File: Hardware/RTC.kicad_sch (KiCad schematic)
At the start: 13 parts

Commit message: add diode
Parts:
- added D? (x3): D_Schottky, symbol IVS_SYMBOL_DIR:D_Schottky
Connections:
- net +3V3: now also D?.1, D?.1
- net at IC?.14 (VBAT): now also D?.2, D?.2
- net at BT?.1 (+), R?.1, R?.2: now also D?.2
- net at BT?.1 (+): now also D?.1
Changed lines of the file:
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@@
   (junction (at 80.01 67.31) (diameter 0) (color 0 0 0 0)
+  )
+  (junction (at 113.03 88.9) (diameter 0) (color 0 0 0 0)
   )
   (junction (at 97.79 88.9) (diameter 0) (color 0 0 0 0)
@@
     (stroke (width 0) (type default) (color 0 0 0 0))
   )
-  (wire (pts (xy 100.33 88.9) (xy 109.22 88.9))
+  (wire (pts (xy 100.33 88.9) (xy 113.03 88.9))
     (stroke (width 0) (type default) (color 0 0 0 0))
   )
@@
     (stroke (width 0) (type default) (color 0 0 0 0))
   )
+  (wire (pts (xy 113.03 96.52) (xy 119.38 96.52))
+    (stroke (width 0) (type default) (color 0 0 0 0))
+  )
   (wire (pts (xy 76.2 106.68) (xy 87.63 106.68))
     (stroke (width 0) (type default) (color 0 0 0 0))
@@
     (stroke (width 0) (type default) (color 0 0 0 0))
   )
-  (wire (pts (xy 116.84 88.9) (xy 125.73 88.9))
-    (stroke (width 0) (type default) (color 0 0 0 0))
-  )
   (wire (pts (xy 85.09 57.785) (xy 86.36 57.785))
     (stroke (width 0) (type default) (color 0 0 0 0))
@@
     (stroke (width 0) (type default) (color 0 0 0 0))
   )
+  (wire (pts (xy 120.65 88.9) (xy 125.73 88.9))
+    (stroke (width 0) (type default) (color 0 0 0 0))
+  )
   (wire (pts (xy 97.79 87.63) (xy 97.79 88.9))
     (stroke (width 0) (type default) (color 0 0 0 0))
@@
   )
   (wire (pts (xy 83.82 88.9) (xy 83.82 92.71))
-    (stroke (width 0) (type default) (color 0 0 0 0))
-  )
-  (wire (pts (xy 107.95 96.52) (xy 119.38 96.52))
     (stroke (width 0) (type default) (color 0 0 0 0))
   )
@@
     (effects (font (size 1.27 1.27)) (justify left))
   )
+  (symbol (lib_id "IVS_SYMBOL_DIR:D_Schottky") (at 115.57 88.9 0) (unit 1)
+    (in_bom yes) (on_board yes) (fields_autoplaced)
+    (property "Reference" "D?" (id 0) (at 116.5394 82.55 0))
+    (property "Value" "D_Schottky" (id 1) (at 116.5394 85.09 0))
+    (property "Footprint" "" (id 2) (at 115.57 88.9 0)
+      (effects (font (size 1.27 1.27)) hide)
+    )
+    (property "Datasheet" "" (id 3) (at 115.57 88.9 0)
+      (effects (font (size 1.27 1.27)) hide)
+    )
+    (pin "1")
+    (pin "2")
+  )
   (symbol (lib_id "power:GND") (at 119.38 107.95 0) (unit 1)
     (in_bom yes) (on_board yes) (fields_autoplaced)
@@
     )
     (pin "1")
+  )
+  (symbol (lib_id "IVS_SYMBOL_DIR:D_Schottky") (at 113.03 91.44 270) (unit 1)
+    (in_bom yes) (on_board yes) (fields_autoplaced)
+    (property "Reference" "D?" (id 0) (at 115.57 91.1393 90)
+      (effects (font (size 1.27 1.27)) (justify left))
+    )
+    (property "Value" "D_Schottky" (id 1) (at 115.57 93.6793 90)
+      (effects (font (size 1.27 1.27)) (justify left))
+    )
+    (property "Footprint" "" (id 2) (at 113.03 91.44 0)
+      (effects (font (size 1.27 1.27)) hide)
+    )
+    (property "Datasheet" "" (id 3) (at 113.03 91.44 0)
+      (effects (font (size 1.27 1.27)) hide)
+    )
+    (pin "1")
+    (pin "2")
   )
   (symbol (lib_id "Device:Crystal") (at 74.93 50.8 90) (unit 1)
@@
       (effects (font (size 1.27 1.27)) hide)
     )
+    (pin "1")
+    (pin "2")
+  )
+  (symbol (lib_id "IVS_SYMBOL_DIR:D_Schottky") (at 91.44 67.31 0) (unit 1)
+    (in_bom yes) (on_board yes)
+    (property "Reference" "D?" (id 0) (at 92.71 64.77 0))
+    (property "Value" "D_Schottky" (id 1) (at 92.71 69.85 0))
+    (property "Footprint" "" (id 2) (at 91.44 67.31 0)
+      (effects (font (size 1.27 1.27)) hide)
+    )
+    (property "Datasheet" "" (id 3) (at 91.44 67.31 0)
+      (effects (font (size 1.27 1.27)) hide)
+    )

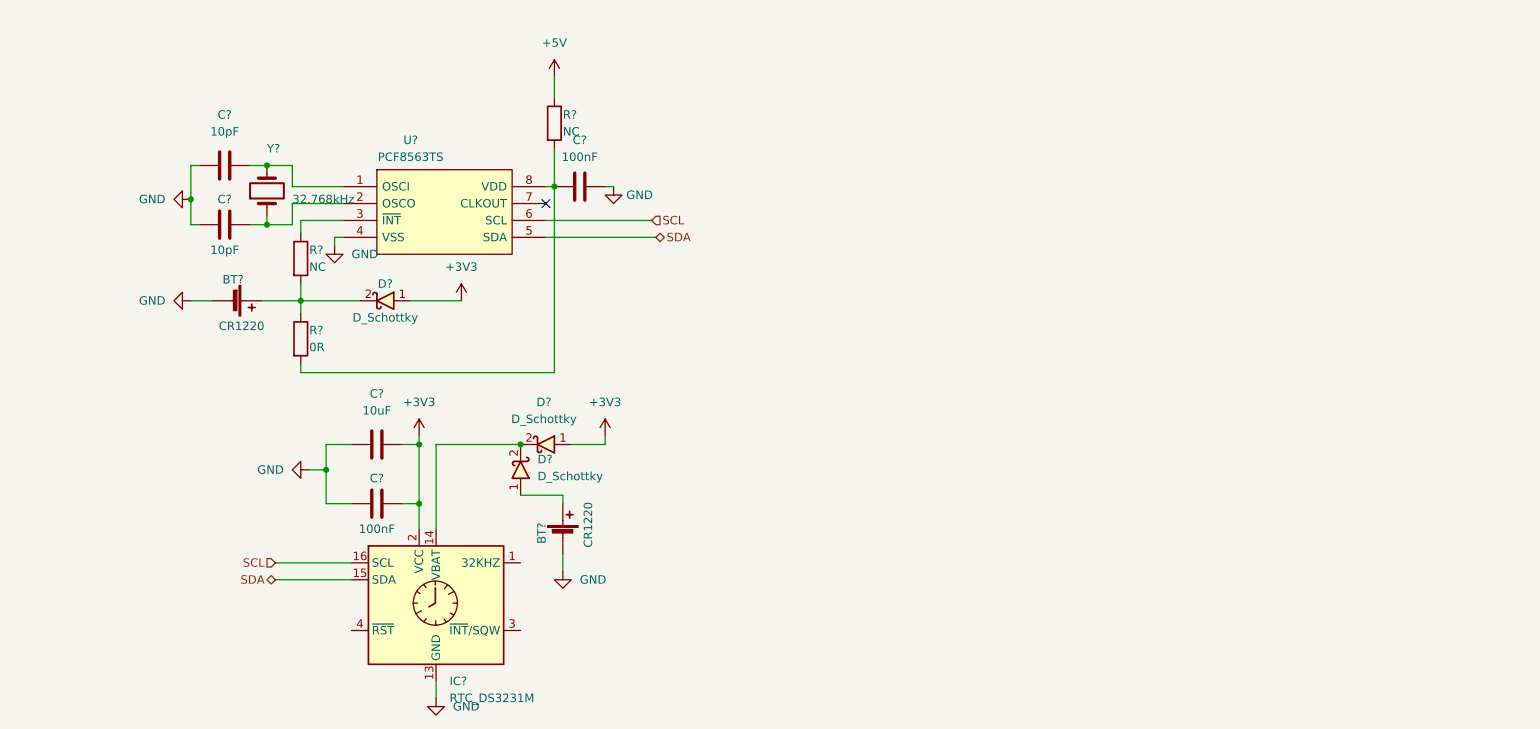
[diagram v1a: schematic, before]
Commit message: remove crytals 32kHz and add Potentiometer in mcp41010
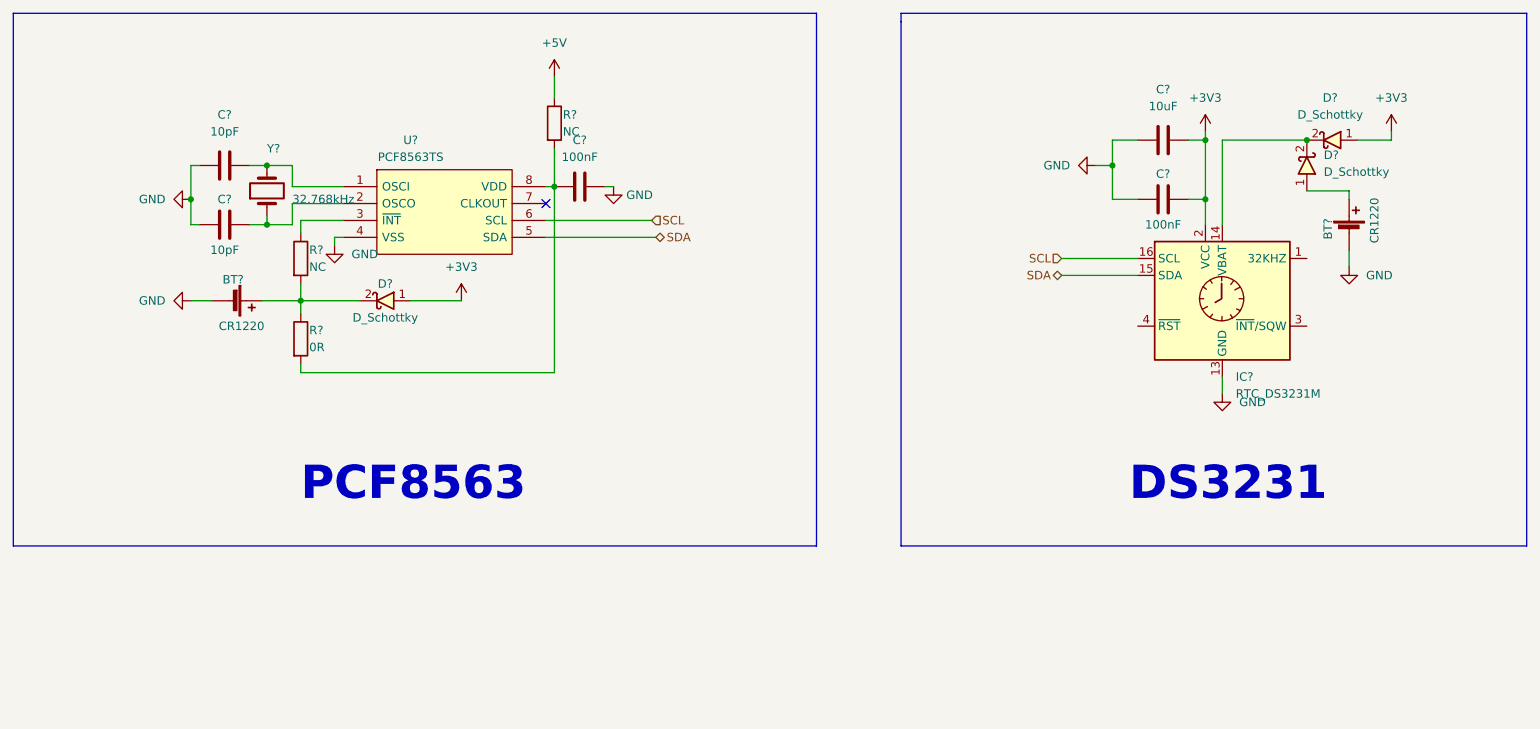
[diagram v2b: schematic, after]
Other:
- note added: "DS3231"
- note added: "PCF8563"
- moved on the sheet: BT?, C?, D?, IC?

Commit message: after merge dev
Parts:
- U7: renamed from U?; footprint project:SOIC127P600X175-8N -> IVS_FOOTPRINTS:SOIC-8
- gave numbers to parts that had none: 15
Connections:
- net SCL renamed i2c.SCL
- net SDA renamed i2c.SDA

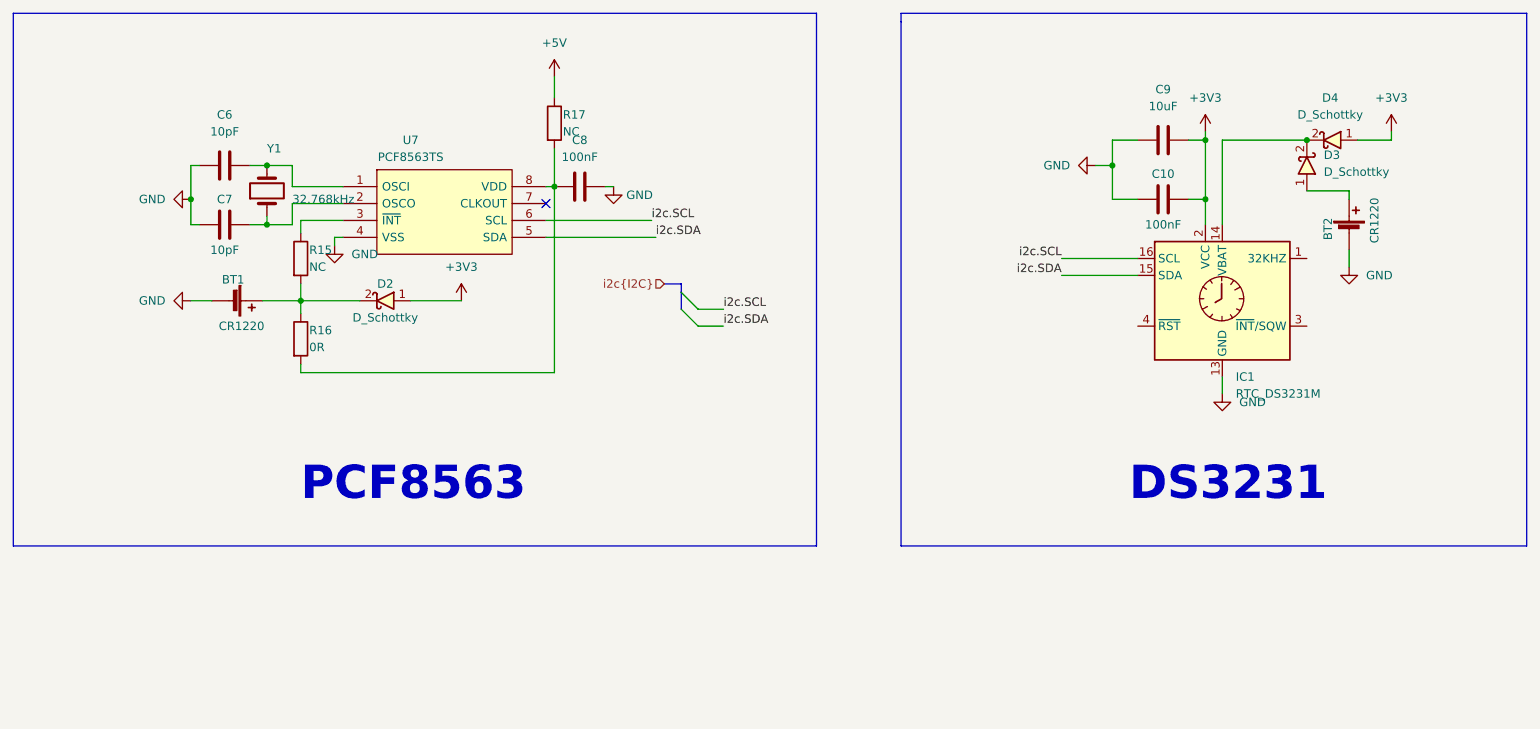
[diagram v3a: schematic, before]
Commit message: remove 1 batery in RTC block
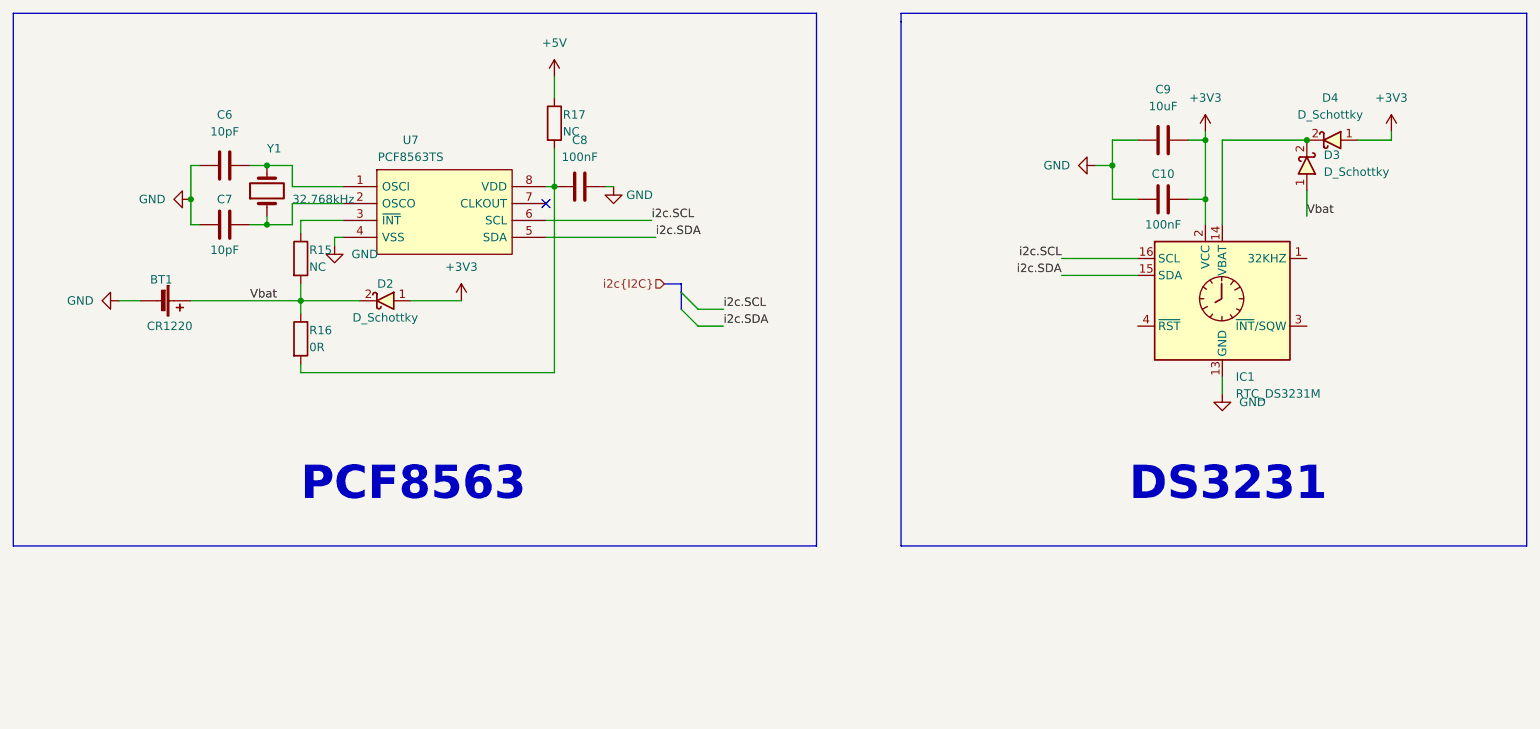
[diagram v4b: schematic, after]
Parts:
- removed BT2: CR1220, symbol Device:Battery_Cell
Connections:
- net Vbat: now reaches D3.1
- net Vbat: now also BT1.1 (+), D2.2, R15.2, R16.1
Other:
- moved on the sheet: BT1
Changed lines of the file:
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@@
     (stroke (width 0) (type default) (color 0 0 0 0))
   )
-  (wire (pts (xy 231.14 50.8) (xy 237.49 50.8))
+  (wire (pts (xy 231.14 50.8) (xy 231.14 54.61))
     (stroke (width 0) (type default) (color 0 0 0 0))
   )
@@
     (stroke (width 0) (type default) (color 0 0 0 0))
   )
-  (wire (pts (xy 237.49 50.8) (xy 237.49 52.07))
-    (stroke (width 0) (type default) (color 0 0 0 0))
-  )
   (wire (pts (xy 78.74 46.99) (xy 78.74 50.165))
     (stroke (width 0) (type default) (color 0 0 0 0))
@@
     (stroke (width 0) (type default) (color 0 0 0 0))
   )
-  (wire (pts (xy 74.295 67.31) (xy 80.01 67.31))
+  (wire (pts (xy 63.5 67.31) (xy 80.01 67.31))
     (stroke (width 0) (type default) (color 0 0 0 0))
   )
@@
     (stroke (width 0) (type default) (color 0 0 0 0))
   )
-  (wire (pts (xy 66.675 67.31) (xy 63.5 67.31))
+  (wire (pts (xy 55.88 67.31) (xy 52.705 67.31))
     (stroke (width 0) (type default) (color 0 0 0 0))
   )
@@
   )
   (wire (pts (xy 243.84 43.18) (xy 243.84 41.91))
-    (stroke (width 0) (type default) (color 0 0 0 0))
-  )
-  (wire (pts (xy 237.49 62.23) (xy 237.49 59.69))
     (stroke (width 0) (type default) (color 0 0 0 0))
   )
@@
   (text "DS3231\n" (at 204.47 97.79 0)
     (effects (font (size 5 5) bold) (justify left bottom))
+  )
+  (label "Vbat" (at 72.39 67.31 0)
+    (effects (font (size 1.27 1.27)) (justify left bottom))
+  )
+  (label "Vbat" (at 231.14 54.61 0)
+    (effects (font (size 1.27 1.27)) (justify left bottom))
   )
   (label "i2c.SCL" (at 143.51 68.58 0)
@@
     (pin "1")
     (pin "2")
-  )
-  (symbol (lib_id "power:GND") (at 237.49 62.23 0) (unit 1)
-    (in_bom yes) (on_board yes) (fields_autoplaced)
-    (property "Reference" "#PWR0136" (id 0) (at 237.49 68.58 0)
-      (effects (font (size 1.27 1.27)) hide)
-    )
-    (property "Value" "GND" (id 1) (at 240.03 63.4999 0)
-      (effects (font (size 1.27 1.27)) (justify left))
-    )
-    (property "Footprint" "" (id 2) (at 237.49 62.23 0)
-      (effects (font (size 1.27 1.27)) hide)
-    )
-    (property "Datasheet" "" (id 3) (at 237.49 62.23 0)
-      (effects (font (size 1.27 1.27)) hide)
-    )
-    (pin "1")
   )
   (symbol (lib_id "IVS_SYMBOL_DIR:D_Schottky") (at 231.14 45.72 270) (unit 1)
@@
     (pin "1")
   )
-  (symbol (lib_id "Device:Battery_Cell") (at 69.215 67.31 270) (unit 1)
-    (in_bom yes) (on_board yes)
-    (property "Reference" "BT1" (id 0) (at 69.85 64.135 90))
-    (property "Value" "CR1220" (id 1) (at 71.12 71.12 90))
-    (property "Footprint" "" (id 2) (at 70.739 67.31 90)
-      (effects (font (size 1.27 1.27)) hide)
-    )
-    (property "Datasheet" "~" (id 3) (at 70.739 67.31 90)
+  (symbol (lib_id "Device:Battery_Cell") (at 58.42 67.31 270) (unit 1)
+    (in_bom yes) (on_board yes)
+    (property "Reference" "BT1" (id 0) (at 59.055 64.135 90))
+    (property "Value" "CR1220" (id 1) (at 60.325 71.12 90))
+    (property "Footprint" "" (id 2) (at 59.944 67.31 90)
+      (effects (font (size 1.27 1.27)) hide)
+    )
+    (property "Datasheet" "~" (id 3) (at 59.944 67.31 90)
       (effects (font (size 1.27 1.27)) hide)
     )
@@
     (pin "1")
   )
-  (symbol (lib_id "Device:Battery_Cell") (at 237.49 57.15 0) (unit 1)
-    (in_bom yes) (on_board yes)
-    (property "Reference" "BT2" (id 0) (at 234.315 56.515 90))
-    (property "Value" "CR1220" (id 1) (at 241.3 55.245 90))
-    (property "Footprint" "" (id 2) (at 237.49 55.626 90)
-      (effects (font (size 1.27 1.27)) hide)
-    )
-    (property "Datasheet" "~" (id 3) (at 237.49 55.626 90)
-      (effects (font (size 1.27 1.27)) hide)
-    )
-    (pin "1")
-    (pin "2")
-  )
   (symbol (lib_id "power:+3V3") (at 104.14 67.31 0) (unit 1)
     (in_bom yes) (on_board yes) (fields_autoplaced)
@@
     (pin "2")
   )
-  (symbol (lib_id "power:GND") (at 63.5 67.31 270) (unit 1)
-    (in_bom yes) (on_board yes) (fields_autoplaced)
-    (property "Reference" "#PWR0139" (id 0) (at 57.15 67.31 0)
-      (effects (font (size 1.27 1.27)) hide)
-    )
-    (property "Value" "GND" (id 1) (at 59.69 67.3099 90)
+  (symbol (lib_id "power:GND") (at 52.705 67.31 270) (unit 1)
+    (in_bom yes) (on_board yes) (fields_autoplaced)
+    (property "Reference" "#PWR0139" (id 0) (at 46.355 67.31 0)
+      (effects (font (size 1.27 1.27)) hide)
+    )
+    (property "Value" "GND" (id 1) (at 48.895 67.3099 90)
       (effects (font (size 1.27 1.27)) (justify right))
     )
-    (property "Footprint" "" (id 2) (at 63.5 67.31 0)
-      (effects (font (size 1.27 1.27)) hide)
-    )
-    (property "Datasheet" "" (id 3) (at 63.5 67.31 0)
-      (effects (font (size 1.27 1.27)) hide)
-    )
+    (property "Footprint" "" (id 2) (at 52.705 67.31 0)
+      (effects (font (size 1.27 1.27)) hide)
+    )
+    (property "Datasheet" "" (id 3) (at 52.705 67.31 0)
+      (effects (font (size 1.27 1.27)) hide)
+    )

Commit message: add R0603 footprint
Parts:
- BT1: footprint (none) -> IVS_FOOTPRINTS:BatteryHolder_CR1220
- C10, C6, C7, C8, C9: footprint (none) -> IVS_FOOTPRINTS:C0603
- R15, R16, R17: footprint (none) -> IVS_FOOTPRINTS:R0603
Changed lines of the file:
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@@
     (property "Reference" "C10" (id 0) (at 209.55 48.26 90))
     (property "Value" "100nF" (id 1) (at 209.55 55.88 90))
-    (property "Footprint" "" (id 2) (at 213.36 51.1048 0)
+    (property "Footprint" "IVS_FOOTPRINTS:C0603" (id 2) (at 213.36 51.1048 0)
       (effects (font (size 1.27 1.27)) hide)
     )
@@
     (property "Reference" "C7" (id 0) (at 68.58 52.07 90))
     (property "Value" "10pF" (id 1) (at 68.58 59.69 90))
-    (property "Footprint" "" (id 2) (at 72.39 54.9148 0)
+    (property "Footprint" "IVS_FOOTPRINTS:C0603" (id 2) (at 72.39 54.9148 0)
       (effects (font (size 1.27 1.27)) hide)
     )
@@
     (property "Reference" "BT1" (id 0) (at 59.055 64.135 90))
     (property "Value" "CR1220" (id 1) (at 60.325 71.12 90))
-    (property "Footprint" "" (id 2) (at 59.944 67.31 90)
+    (property "Footprint" "IVS_FOOTPRINTS:BatteryHolder_CR1220" (id 2) (at 59.944 67.31 90)
       (effects (font (size 1.27 1.27)) hide)
     )
@@
       (effects (font (size 1.27 1.27)) (justify left))
     )
-    (property "Footprint" "" (id 2) (at 116.332 40.64 90)
+    (property "Footprint" "IVS_FOOTPRINTS:R0603" (id 2) (at 116.332 40.64 90)
       (effects (font (size 1.27 1.27)) hide)
     )
@@
     (property "Reference" "C8" (id 0) (at 121.92 43.18 90))
     (property "Value" "100nF" (id 1) (at 121.92 45.72 90))
-    (property "Footprint" "" (id 2) (at 125.73 49.1998 0)
+    (property "Footprint" "IVS_FOOTPRINTS:C0603" (id 2) (at 125.73 49.1998 0)
       (effects (font (size 1.27 1.27)) hide)
     )
@@
     (property "Reference" "C9" (id 0) (at 209.55 35.56 90))
     (property "Value" "10uF" (id 1) (at 209.55 38.1 90))
-    (property "Footprint" "" (id 2) (at 213.36 42.2148 0)
+    (property "Footprint" "IVS_FOOTPRINTS:C0603" (id 2) (at 213.36 42.2148 0)
       (effects (font (size 1.27 1.27)) hide)
     )
@@
       (effects (font (size 1.27 1.27)) (justify left))
     )
-    (property "Footprint" "" (id 2) (at 78.232 60.96 90)
+    (property "Footprint" "IVS_FOOTPRINTS:R0603" (id 2) (at 78.232 60.96 90)
       (effects (font (size 1.27 1.27)) hide)
     )
@@
     (property "Reference" "C6" (id 0) (at 68.58 39.37 90))
     (property "Value" "10pF" (id 1) (at 68.58 41.91 90))
-    (property "Footprint" "" (id 2) (at 72.39 46.0248 0)
+    (property "Footprint" "IVS_FOOTPRINTS:C0603" (id 2) (at 72.39 46.0248 0)
       (effects (font (size 1.27 1.27)) hide)
     )
@@
       (effects (font (size 1.27 1.27)) (justify left))
     )
-    (property "Footprint" "" (id 2) (at 78.232 73.025 90)
-      (effects (font (size 1.27 1.27)) hide)
-    )
+    (property "Footprint" "IVS_FOOTPRINTS:R0603" (id 2) (at 78.232 73.025 90)
+      (effects (font (size 1.27 1.27)) hide)
+    )
